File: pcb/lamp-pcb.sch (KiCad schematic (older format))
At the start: 32 parts, among them IC1 ATMEGA328P, IC2 LM1117, IC3 TLC5973, J1 7-12V_OUT, J2 LED_CARD_BOTTOM, P1 7-12V_IN, P2 AVR_ISP, P3 SERIAL, P4 LEDSTACK, P5 LEDSTACK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

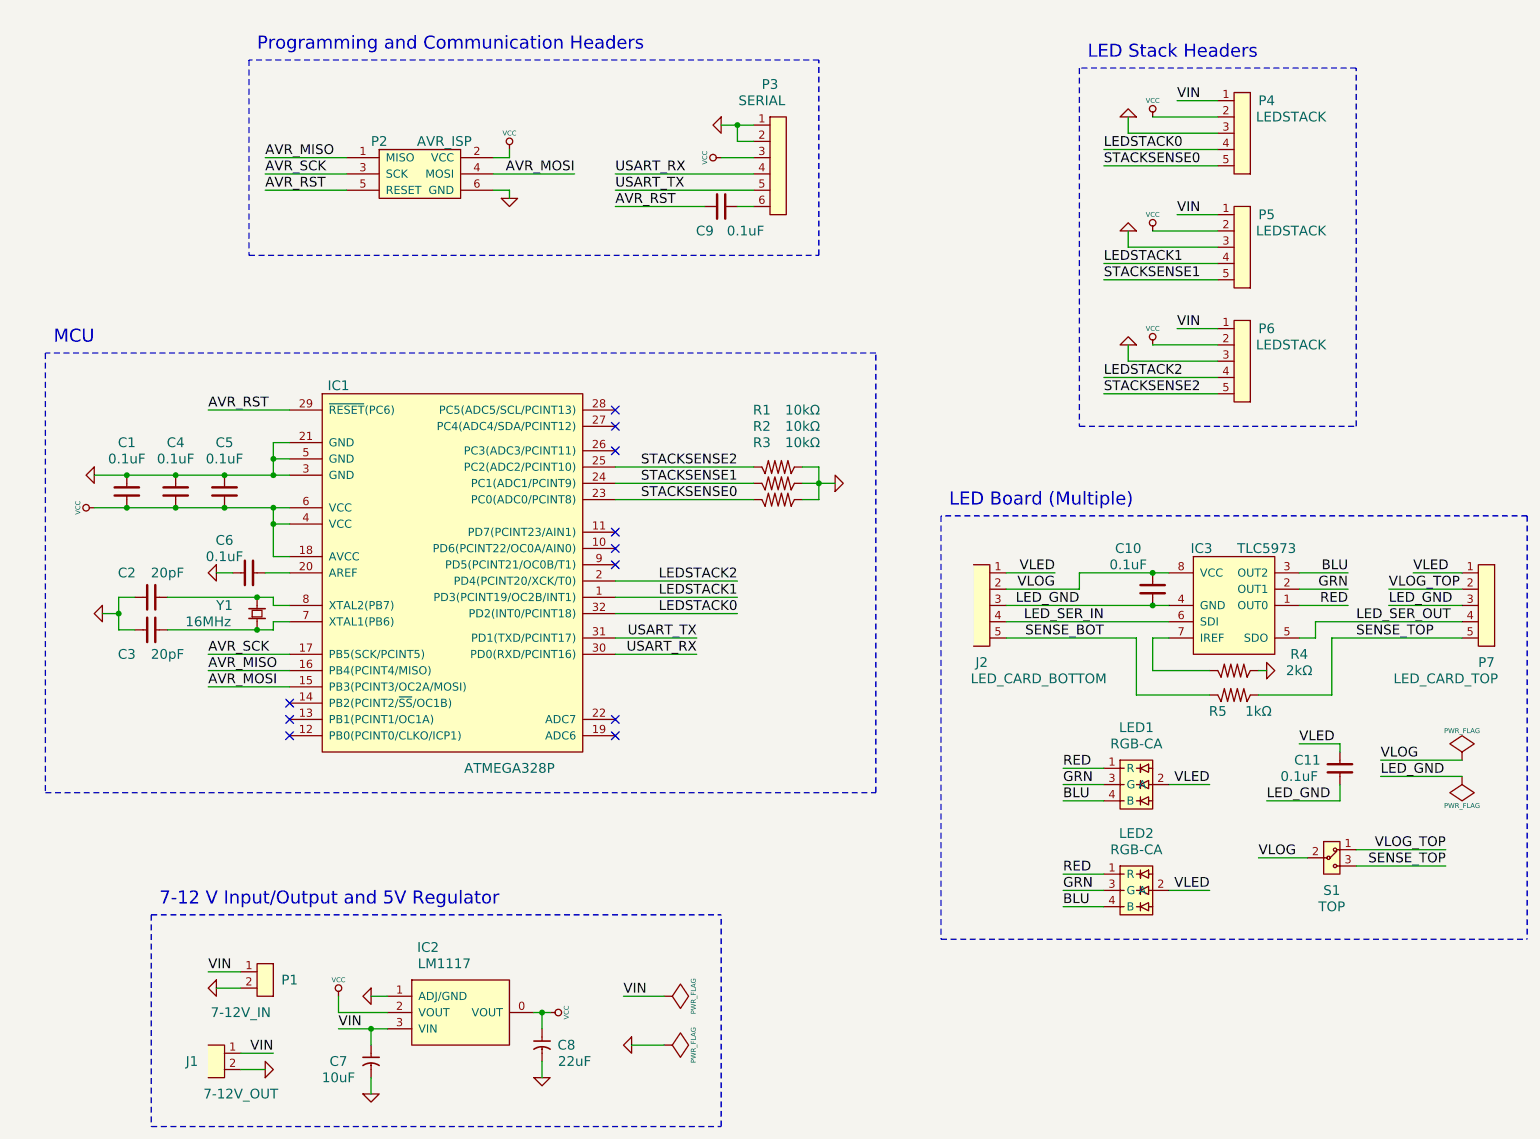
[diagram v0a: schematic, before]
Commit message: footprint selection done; moving to layout
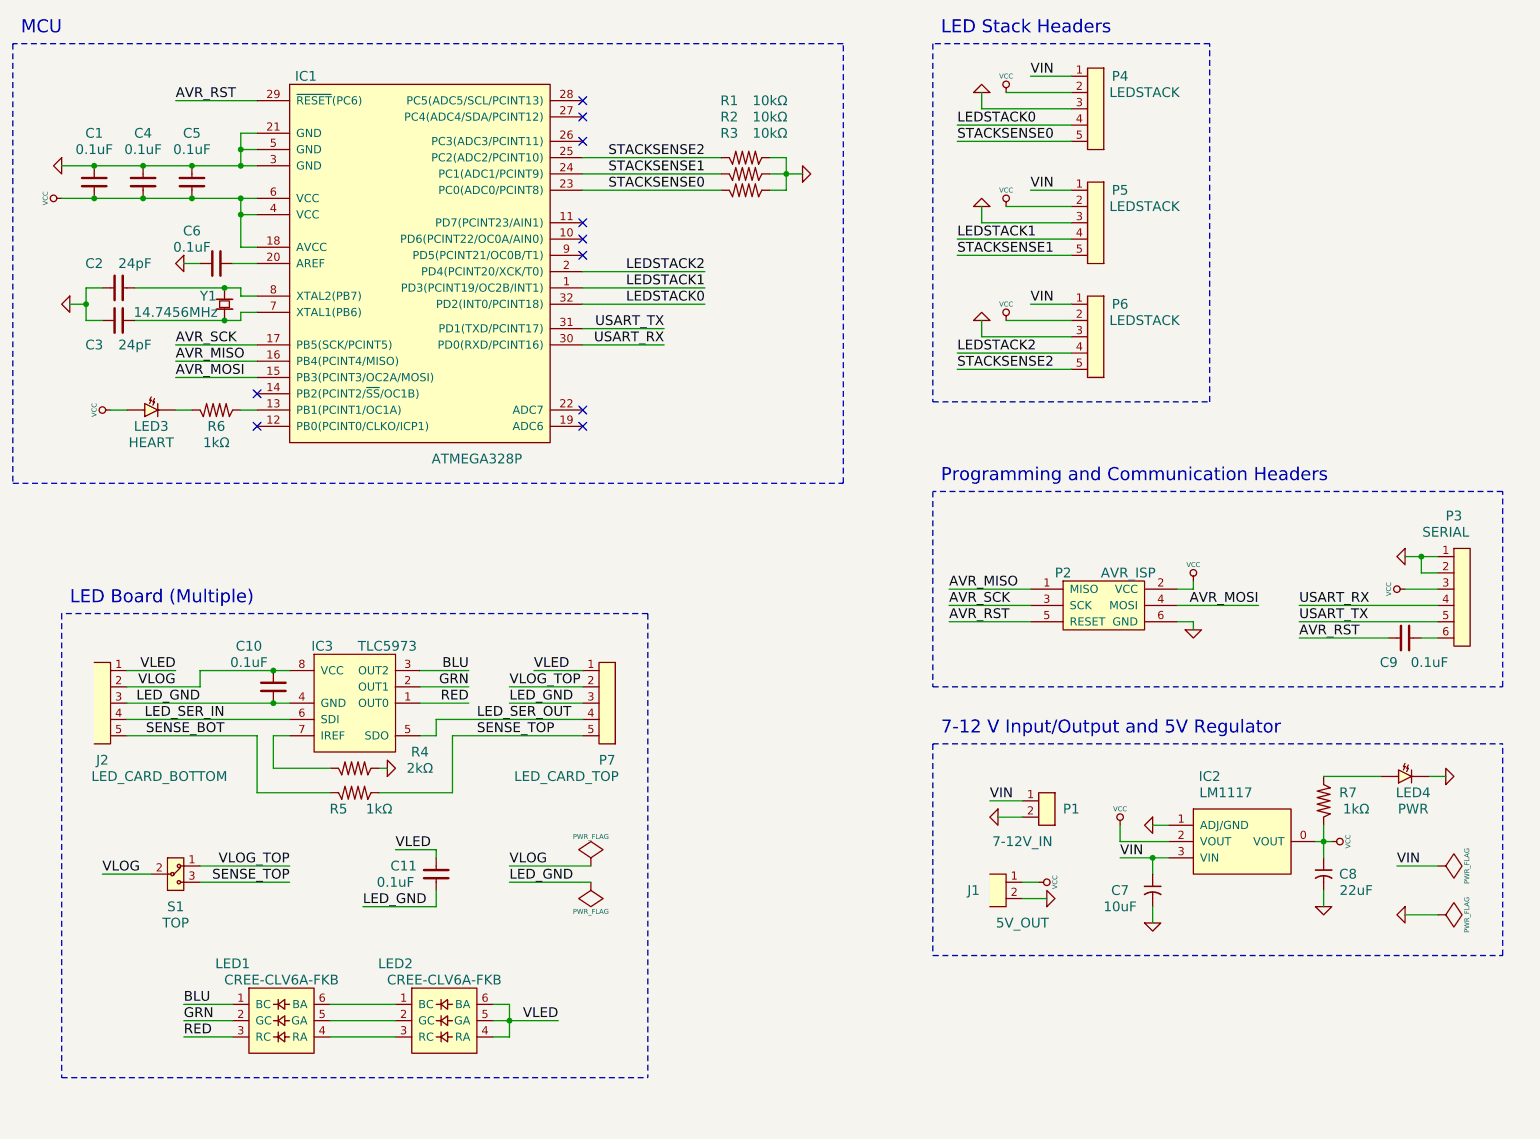
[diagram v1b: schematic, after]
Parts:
- removed LED1, LED2: RGB-CA, symbol LED_RGB-CA
- added LED1, LED2: CREE-CLV6A-FKB, symbol CREE-CLV6A-FKB
- added LED3: HEART, symbol LED
- added LED4: PWR, symbol LED
- added R6, R7: 1kΩ, symbol R
- C1: Distributor (none) -> On Hand
- C10, C11, C4, C5, C6, C9, R1, R2, R3, R4, R5: Distributor (none) -> On hand
- C2, C3: value 20pF -> 24pF; Distrib. Link (none) -> http://www.digikey.com/product-detail/en/CL10C240JB8NCNC/12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; Distrib. Part (none) -> 1276-2242-1-ND; Distributor (none) -> Digikey; Manuf. Part (none) -> CL10C240JB8NCNC; Manufacturer (none) -> Samsung Electro-Mechanics America, Inc
- C7: Distrib. Link (none) -> http://www.digikey.com/product-detail/en/TMK316F106ZL-T/587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; Distrib. Part (none) -> 587-1353-1-ND; Distributor (none) -> Digikey; Manuf. Part (none) -> TMK316F106ZL-T; Manufacturer (none) -> Taiyo Yuden
- C8: Distrib. Link (none) -> http://www.digikey.com/product-detail/en/LMK316F226ZL-T/587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; Distrib. Part (none) -> 587-1356-1-ND; Distributor (none) -> Digikey; Manuf. Part (none) -> LMK316F226ZL-T; Manufacturer (none) -> Taiyo Yuden
- IC2: Distrib. Link (none) -> http://www.digikey.com/product-detail/en/AZ1117CH-5.0TRG1/A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; Distrib. Part (none) -> AZ1117CH-5.0TRG1DICT-ND; Distributor (none) -> Digikey; Manuf. Part (none) -> AZ1117CH-5.0TRG1; Manufacturer (none) -> Diodes Incorporated
- IC3: Manuf. Part (none) -> TLC5973D; Manufacturer Part TLC5973D -> (none)
- J1: value 7-12V_OUT -> 5V_OUT
- S1: Distrib. Link (none) -> http://www.digikey.com/product-detail/en/JS102011SAQN/401-1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; Distrib. Part (none) -> 401-1999-1-ND; Distributor (none) -> Digikey; Manuf. Part (none) -> JS102011SAQN; Manufacturer (none) -> C&K Components
- Y1: value 16MHz -> 14.7456MHz; Distrib. Link (none) -> http://www.digikey.com/product-detail/en/ABLS-14.7456MHZ-B4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; Distrib. Part (none) -> 535-10223-1-ND; Distributor (none) -> Digikey; Manuf. Part (none) -> ABLS-14.7456MHZ-B4-T; Manufacturer (none) -> Abracon Corporation
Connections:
- net BLU: now also LED1.1 (BC)
- net GND: now also LED4.1 (C)
- net GRN: now also LED1.2 (GC)
- net RED: now also LED1.3 (RC)
- net VCC: now also J1.1, LED3.2 (A), R7.1
- net VIN: no longer J1.1
- net VLED: now also LED2.4 (RA), LED2.5 (GA), LED2.6 (BA)
- net at IC1.13 (PB1(PCINT1/OC1A)): now also R6.2
- new net: LED1.4 (RA), LED2.3 (RC)
- new net: LED1.5 (GA), LED2.2 (GC)
- new net: LED1.6 (BA), LED2.1 (BC)
- new net: LED3.1 (C), R6.1
- new net: LED4.2 (A), R7.2
- no-connect marks 11 -> 10
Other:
- moved on the sheet: C1, C10, C11, C2, C4, C5, C6, C7, C8, C9, IC1, IC2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

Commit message: component positions good. need some mounting holes
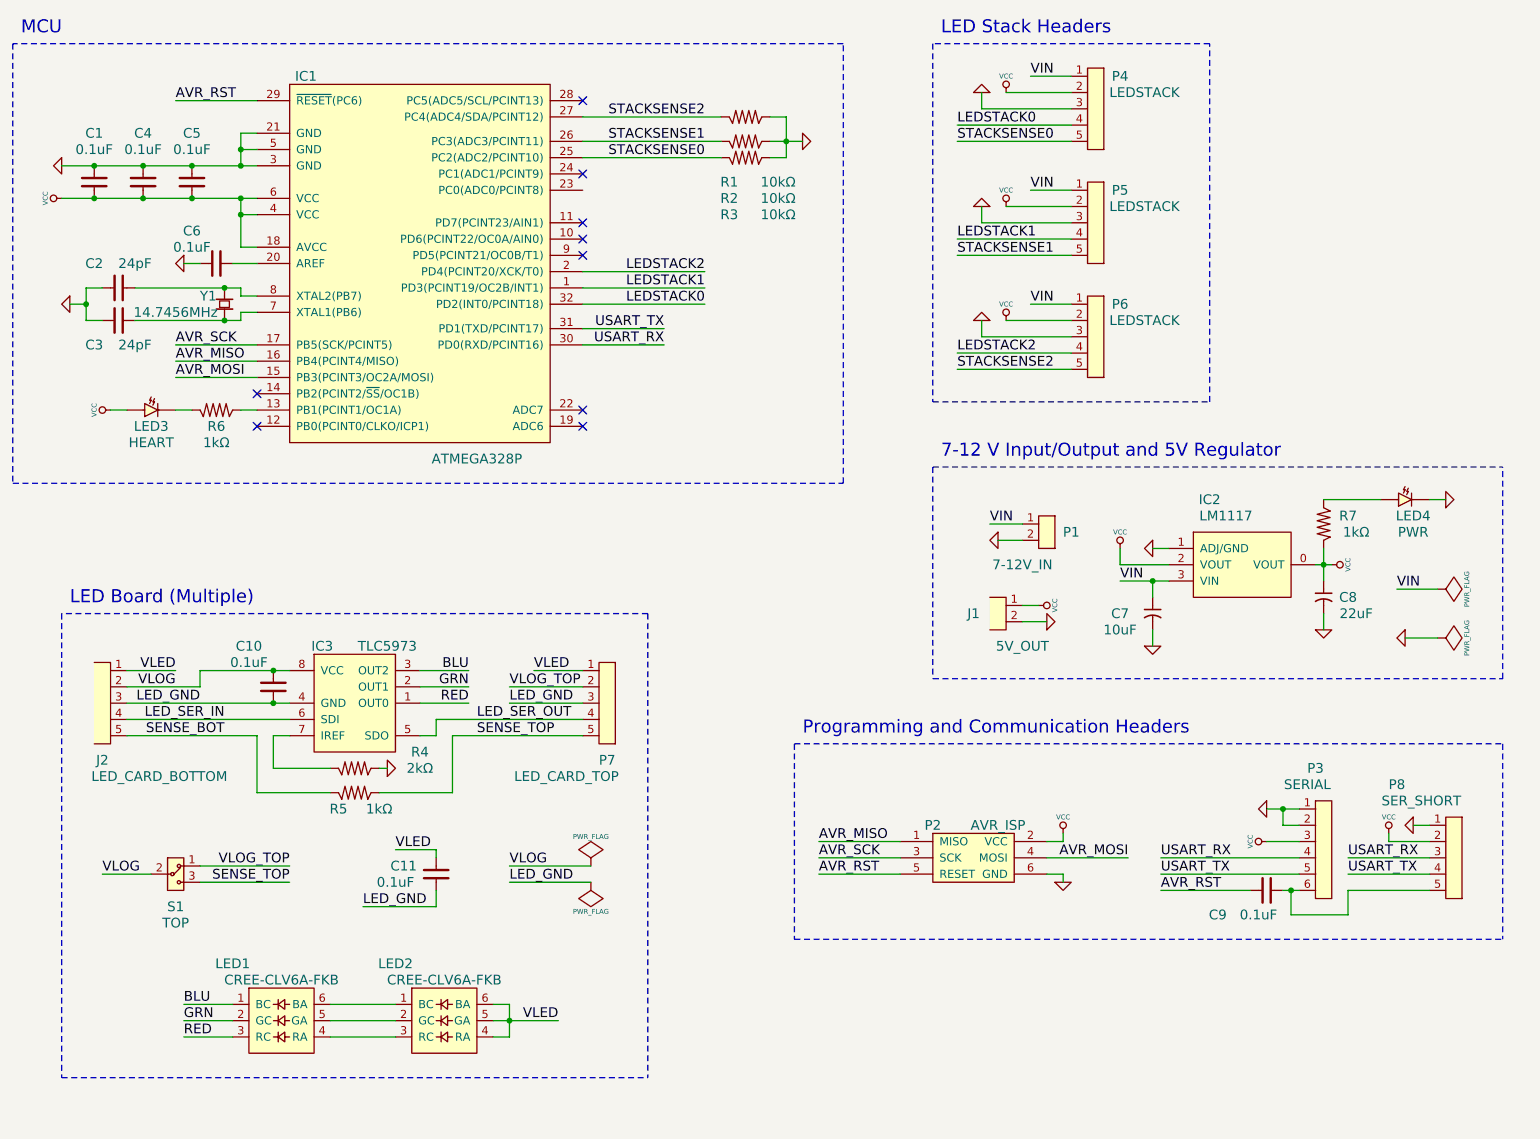
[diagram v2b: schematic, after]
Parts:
- added P8: SER_SHORT, symbol 5PIN_MALE
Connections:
- net GND: now also P8.1
- net STACKSENSE0: now also IC1.25 (PC2(ADC2/PCINT10)); no longer IC1.23 (PC0(ADC0/PCINT8))
- net STACKSENSE1: now also IC1.26 (PC3(ADC3/PCINT11)); no longer IC1.24 (PC1(ADC1/PCINT9))
- net STACKSENSE2: now also IC1.27 (PC4(ADC4/SDA/PCINT12)); no longer IC1.25 (PC2(ADC2/PCINT10))
- net USART_RX: now also P8.3
- net USART_TX: now also P8.4
- net VCC: now also P8.2
- net at C9.2, P3.6: now also P8.5
- no-connect marks 10 -> 9
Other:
- moved on the sheet: C7, C8, C9, IC2, J1, LED4, P1, P2, P3, R1, R2, R3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

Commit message: layout going well but computer dying
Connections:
- net GND: no longer R4.2
- net LED_GND: now also R4.2
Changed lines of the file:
@@
 U 1 1 530E80D0
 P 2950 5350
-F 0 "R4" H 3350 5450 60  0000 C CNN
-F 1 "2kΩ" H 3350 5350 60  0000 C CNN
+F 0 "R4" H 2750 5300 60  0000 C CNN
+F 1 "2kΩ" H 3150 5300 60  0000 C CNN
 F 2 "" H 2950 5350 60  0001 C CNN
 F 3 "" H 2950 5350 60  0001 C CNN
@@
 	1    2950 5500
 	1    0    0    -1
-$EndComp
-$Comp
-L GND #PWR022
-U 1 1 530E89BC
-P 3150 5350
-F 0 "#PWR022" H 3150 5350 30  0001 C CNN
-F 1 "GND" H 3150 5280 30  0001 C CNN
-F 2 "" H 3150 5350 60  0000 C CNN
-F 3 "" H 3150 5350 60  0000 C CNN
-	1    3150 5350
-	0    -1   -1   0
 $EndComp
 $Comp
@@
 $EndComp
 $Comp
-L GND #PWR023
+L GND #PWR022
 U 1 1 530E9AF9
 P 7200 4450
-F 0 "#PWR023" H 7200 4450 30  0001 C CNN
+F 0 "#PWR022" H 7200 4450 30  0001 C CNN
 F 1 "GND" H 7200 4380 30  0001 C CNN
 F 2 "" H 7200 4450 60  0000 C CNN
@@
 	3350 5150 3450 5150
 Wire Wire Line
-	3150 5350 3100 5350
+	3100 5350 3500 5350
 Wire Wire Line
 	3350 4750 3650 4750
@@
 	1400 6000 1700 6000
 $Comp
-L PWR_FLAG #FLG024
+L PWR_FLAG #FLG023
 U 1 1 530EAF0C
 P 9600 4250
-F 0 "#FLG024" H 9600 4345 30  0001 C CNN
+F 0 "#FLG023" H 9600 4345 30  0001 C CNN
 F 1 "PWR_FLAG" H 9600 4430 30  0000 C CNN
 F 2 "" H 9600 4250 60  0000 C CNN
@@
 $EndComp
 $Comp
-L PWR_FLAG #FLG025
+L PWR_FLAG #FLG024
 U 1 1 530EAF4D
 P 9600 4550
-F 0 "#FLG025" H 9600 4645 30  0001 C CNN
+F 0 "#FLG024" H 9600 4645 30  0001 C CNN
 F 1 "PWR_FLAG" H 9600 4730 30  0000 C CNN
 F 2 "" H 9600 4550 60  0000 C CNN
@@
 	9350 4250 9600 4250
 $Comp
-L GND #PWR026
+L GND #PWR025
 U 1 1 530EB006
 P 9400 4550
-F 0 "#PWR026" H 9400 4550 30  0001 C CNN
+F 0 "#PWR025" H 9400 4550 30  0001 C CNN
 F 1 "GND" H 9400 4480 30  0001 C CNN
 F 2 "" H 9400 4550 60  0000 C CNN
@@
 LED_GND
 $Comp
-L PWR_FLAG #FLG027
+L PWR_FLAG #FLG026
 U 1 1 530EB2B1
 P 4400 6050
-F 0 "#FLG027" H 4400 6145 30  0001 C CNN
+F 0 "#FLG026" H 4400 6145 30  0001 C CNN
 F 1 "PWR_FLAG" H 4400 6230 30  0000 C CNN
 F 2 "" H 4400 6050 60  0000 C CNN
@@
 VLOG
 $Comp
-L PWR_FLAG #FLG028
+L PWR_FLAG #FLG027
 U 1 1 530EB2DC
 P 4400 5950
-F 0 "#FLG028" H 4400 6045 30  0001 C CNN
+F 0 "#FLG027" H 4400 6045 30  0001 C CNN
 F 1 "PWR_FLAG" H 4400 6130 30  0000 C CNN
 F 2 "" H 4400 5950 60  0000 C CNN
@@
 $EndComp
 $Comp
-L VCC #PWR029
+L VCC #PWR028
 U 1 1 5310DE0A
 P 7150 4350
-F 0 "#PWR029" H 7150 4450 30  0001 C CNN
+F 0 "#PWR028" H 7150 4450 30  0001 C CNN
 F 1 "VCC" H 7150 4450 30  0000 C CNN
 F 2 "" H 7150 4350 60  0000 C CNN
@@
 $EndComp
 $Comp
-L VCC #PWR030
+L VCC #PWR029
 U 1 1 5310FF7B
 P 1450 3150
-F 0 "#PWR030" H 1450 3250 30  0001 C CNN
+F 0 "#PWR029" H 1450 3250 30  0001 C CNN
 F 1 "VCC" H 1450 3250 30  0000 C CNN
 F 2 "" H 1450 3150 60  0000 C CNN
@@
 	8900 3700 9250 3700
 $Comp
-L GND #PWR031
+L GND #PWR030
 U 1 1 531102AD
 P 9650 3700
-F 0 "#PWR031" H 9650 3700 30  0001 C CNN
+F 0 "#PWR030" H 9650 3700 30  0001 C CNN
 F 1 "GND" H 9650 3630 30  0001 C CNN
 F 2 "" H 9650 3700 60  0000 C CNN
@@
 $EndComp
 $Comp
-L GND #PWR032
+L GND #PWR031
 U 1 1 53174FBF
 P 9450 5700
-F 0 "#PWR032" H 9450 5700 30  0001 C CNN
+F 0 "#PWR031" H 9450 5700 30  0001 C CNN
 F 1 "GND" H 9450 5630 30  0001 C CNN
 F 2 "" H 9450 5700 60  0000 C CNN
@@
 $EndComp
 $Comp
-L VCC #PWR033
+L VCC #PWR032
 U 1 1 53174FD3
 P 9300 5750
-F 0 "#PWR033" H 9300 5850 30  0001 C CNN
+F 0 "#PWR032" H 9300 5850 30  0001 C CNN
 F 1 "VCC" H 9300 5850 30  0000 C CNN
 F 2 "" H 9300 5750 60  0000 C CNN
@@
 	5600 1350 5500 1350
 NoConn ~ 4350 1700
+Text Label 3500 5350 2    60   ~ 0
+LED_GND
 $EndSCHEMATC

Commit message: fixing up a few minor bom issues
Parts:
- C2: Manufacturer Samsung Electro-Mechanics America, Inc -> Samsung
- IC1: Distributor (none) -> Digikey; Distributor Link (none) -> http://www.digikey.com/product-detail/en/ATMEGA328P-AU/ATME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; Distributor Part (none) -> ATMEGA328P-AU-ND; Manufacturer (none) -> Atmel; Manufacturer Part (none) -> ATMEGA328P-AU
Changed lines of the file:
@@
 F 2 "" H 3350 2250 60  0000 C CNN
 F 3 "" H 3350 2250 60  0000 C CNN
+F 4 "Atmel" H 3350 2250 60  0001 C CNN "Manufacturer"
+F 5 "ATMEGA328P-AU" H 3350 2250 60  0001 C CNN "Manufacturer Part"
+F 6 "Digikey" H 3350 2250 60  0001 C CNN "Distributor"
+F 7 "ATMEGA328P-AU-ND" H 3350 2250 60  0001 C CNN "Distributor Part"
+F 8 "http://www.digikey.com/product-detail/en/ATMEGA328P-AU/ATMEGA328P-AU-ND/1832260" H 3350 2250 60  0001 C CNN "Distributor Link"
 	1    3350 2250
 	1    0    0    -1
@@
 F 2 "" H 1500 2400 60  0001 C CNN
 F 3 "" H 1500 2400 60  0001 C CNN
-F 4 "Samsung Electro-Mechanics America, Inc" H 1500 2400 60  0001 C CNN "Manufacturer"
+F 4 "Samsung" H 1500 2400 60  0001 C CNN "Manufacturer"
 F 5 "CL10C240JB8NCNC" H 1500 2400 60  0001 C CNN "Manuf. Part"
 F 6 "Digikey" H 1500 2400 60  0001 C CNN "Distributor"
